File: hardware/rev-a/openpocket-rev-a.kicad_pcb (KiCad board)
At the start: 8 copper layers, 115 x 72 mm, 315 parts, among them J1 ER-TFT050A3-2 FFC, J11 5.8 GHz antenna U.FL, J12 push-push microSD, J13 speaker solder pads, J14 SSD1306 128x64 OLED pads, J15 expander developer pads, J18 rotary encoder control pads, J19 ARM switch pads, J2 USB-C, J20 AUX2 three-position switch pa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, J21 AUX3 three-position switch pa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, J22 AUX4 three-position switch pa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, J23 AIL trim pads, J24 ELE trim pads, J25 THR trim pads, J26 RUD trim pads, J3 battery/NTC, J4 speaker connector, J5 master switch, J6 ELRS, J7 left gimbal, J8 right gimbal, J9 menu/UI control pads, Q1 dual protection FET, Q2 Q_BUZZ buzzer MOSFET, U1 ESP32-S3-MINI-1U-N8, U10 display 3V3 buck, U11 analog OSD, U12 OSD 3V3-to-5V, U13 OSD 5V-to-3V3, U14 CVBS TFT controller, U15 AMT boot flash, U16 AMT flash mux, U17 backlight boost, U18 GPIO expander 0x20, U19 GPIO expander 0x21, U2 1S charger/power path, U20 master load switch, U21 I2S speaker amplifier, U22 3V3_SD load switch, U3 1S protector, U4 fuel gauge, U5 3V3 buck-boost, U6 5V boost, U7 5V_VIDEO load switch, U8 5V_DISPLAY load switch, U9 5V_ELRS load switch, Y1 27.000MHz, Y2 27.000MHz

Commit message: fix(rev-a): eliminate placement and silkscreen DRC violations
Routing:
- net AMT_FLASH_C_MISO: track 29.3 -> 0.00 mm, vias 2 -> 0
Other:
- board text removed: "5.8G U.FL"
- board text removed: "DEV IO"

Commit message: route(rev-a): connect U5 output bulk capacitor
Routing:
- net 3V3_LOGIC: track 0.00 -> 5.72 mm, vias 0 -> 1
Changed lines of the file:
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@@
+	)
+	(segment
+		(start 65.4 42.54)
+		(end 67 42)
+		(width 0.4)
+		(layer "F.Cu")
+		(net 2)
+	)
+	(via
+		(at 67 42)
+		(size 0.55)
+		(drill 0.25)
+		(layers "F.Cu" "B.Cu")
+		(tenting front back)
+		(net 2)
+	)
+	(segment
+		(start 67 42)
+		(end 67.035 46.035)
+		(width 0.4)
+		(layer "B.Cu")
+		(net 2)
 	)
 	(segment
@@
 	)
 	(via
-		(at 12.64 63.4)
+		(at 16.35 57.8)
 		(size 0.45)
 		(drill 0.2)
@@
 	)
 	(via
-		(at 16.35 57.8)
+		(at 12.64 63.4)
 		(size 0.45)
 		(drill 0.2)
@@
 	)
 	(segment
-		(start 7.8 66.3)
-		(end 2 66.3)
+		(start 2 66.3)
+		(end 2 43.2)
 		(width 0.4)
 		(layer "In2.Cu")
@@
 	)
 	(segment
-		(start 2 66.3)
-		(end 2 43.2)
+		(start 7.8 66.3)
+		(end 2 66.3)
 		(width 0.4)
 		(layer "In2.Cu")

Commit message: route(rev-a): extend reviewed 3V3 bulk fanout
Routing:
- net 3V3_LOGIC: track 5.72 -> 13.0 mm, vias 1 -> 3
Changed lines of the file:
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@@
+	)
+	(via
+		(at 62 48.5)
+		(size 0.55)
+		(drill 0.25)
+		(layers "F.Cu" "B.Cu")
+		(tenting front back)
+		(net 2)
 	)
 	(via
@@
 		(layers "F.Cu" "B.Cu")
 		(tenting front back)
+		(net 2)
+	)
+	(via
+		(at 66.5 47.5)
+		(size 0.55)
+		(drill 0.25)
+		(layers "F.Cu" "B.Cu")
+		(tenting front back)
+		(net 2)
+	)
+	(segment
+		(start 67.035 46.035)
+		(end 66.5 47.5)
+		(width 0.4)
+		(layer "B.Cu")
+		(net 2)
+	)
+	(segment
+		(start 62 48.5)
+		(end 63 49)
+		(width 0.4)
+		(layer "B.Cu")
 		(net 2)
 	)
@@
 	)
 	(segment
-		(start 16.35 57.8)
-		(end 16.35 56.95)
-		(width 0.3)
-		(layer "F.Cu")
-		(net 49)
+		(start 66.5 47.5)
+		(end 62 48.5)
+		(width 0.4)
+		(layer "In2.Cu")
+		(net 2)
 	)
 	(segment
@@
 		(net 49)
 	)
-	(via
-		(at 16.35 57.8)
-		(size 0.45)
-		(drill 0.2)
-		(layers "F.Cu" "B.Cu")
-		(tenting front back)
+	(segment
+		(start 16.35 57.8)
+		(end 16.35 56.95)
+		(width 0.3)
+		(layer "F.Cu")
 		(net 49)
 	)
@@
 		(net 49)
 	)
+	(via
+		(at 16.35 57.8)
+		(size 0.45)
+		(drill 0.2)
+		(layers "F.Cu" "B.Cu")
+		(tenting front back)
+		(net 49)
+	)
+	(segment
+		(start 12.64 63.4)
+		(end 16.35 57.8)
+		(width 0.4)
+		(layer "In2.Cu")
+		(net 49)
+	)
 	(segment
 		(start 10.6 64.5)
@@
 		(start 10.6 68.4)
 		(end 10.6 64.5)
-		(width 0.4)
-		(layer "In2.Cu")
-		(net 49)
-	)
-	(segment
-		(start 12.64 63.4)
-		(end 16.35 57.8)
 		(width 0.4)
 		(layer "In2.Cu")
@@
 	)
 	(via
+		(at 7.8 68.4)
+		(size 0.45)
+		(drill 0.2)
+		(layers "F.Cu" "B.Cu")
+		(tenting front back)
+		(net 53)
+	)
+	(via
 		(at 2 43.2)
 		(size 0.45)
@@
 		(net 53)
 	)
-	(via
-		(at 7.8 68.4)
-		(size 0.45)
-		(drill 0.2)
-		(layers "F.Cu" "B.Cu")
-		(tenting front back)
+	(segment
+		(start 7.8 66.3)
+		(end 2 66.3)
+		(width 0.4)
+		(layer "In2.Cu")
 		(net 53)
 	)
@@
 		(width 0.4)
 		(layer "In2.Cu")
-		(net 53)
-	)
-	(segment
-		(start 7.8 66.3)
-		(end 2 66.3)
-		(width 0.4)
-		(layer "In2.Cu")

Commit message: route(rev-a): add dedicated 3V3 distribution plane
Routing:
- net 3V3_LOGIC: track 13.0 -> 56.5 mm, vias 3 -> 54
- added copper zone on In5.Cu, net 3V3_LOGIC

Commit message: route(rev-a): add main 5V distribution plane
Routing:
- net SYS_SWITCHED_5V: track 0.00 -> 13.8 mm, vias 0 -> 15
- added copper zone on In2.Cu, net SYS_SWITCHED_5V

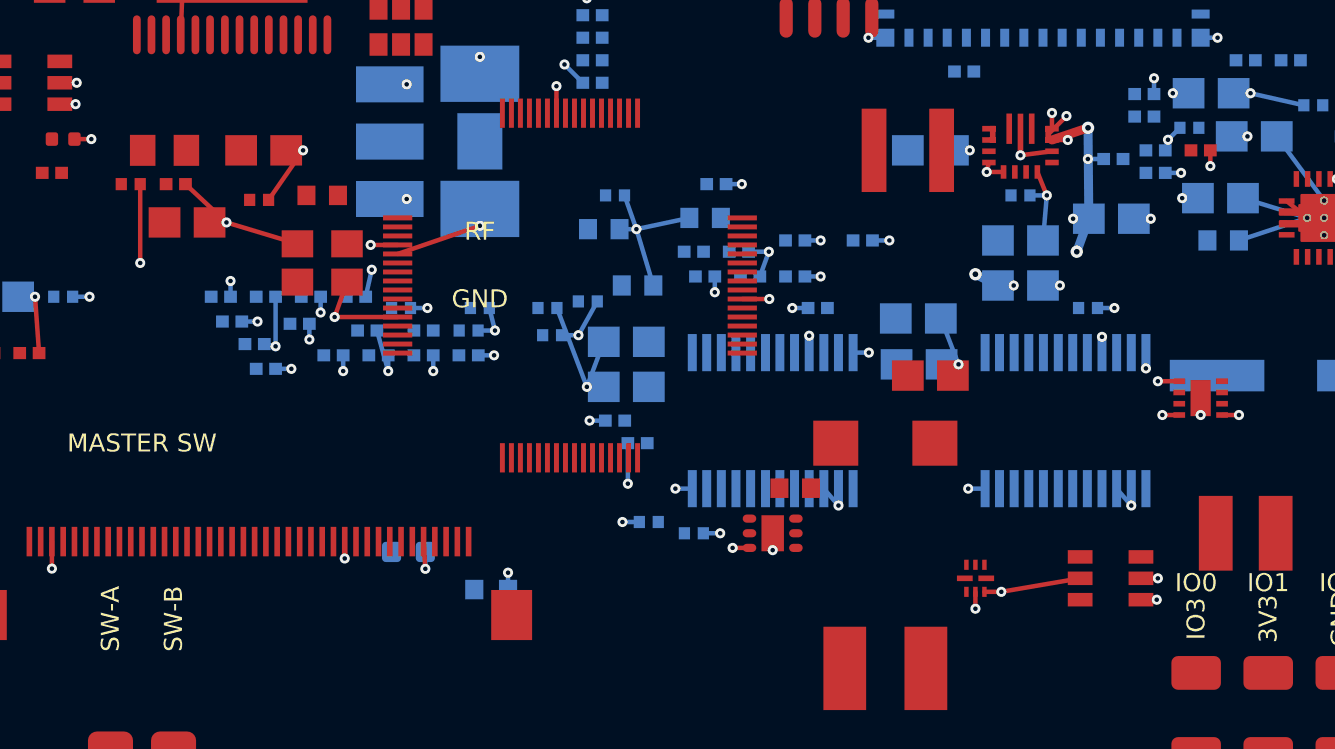
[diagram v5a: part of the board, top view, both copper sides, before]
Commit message: place(rev-a): cluster master switch with power converters
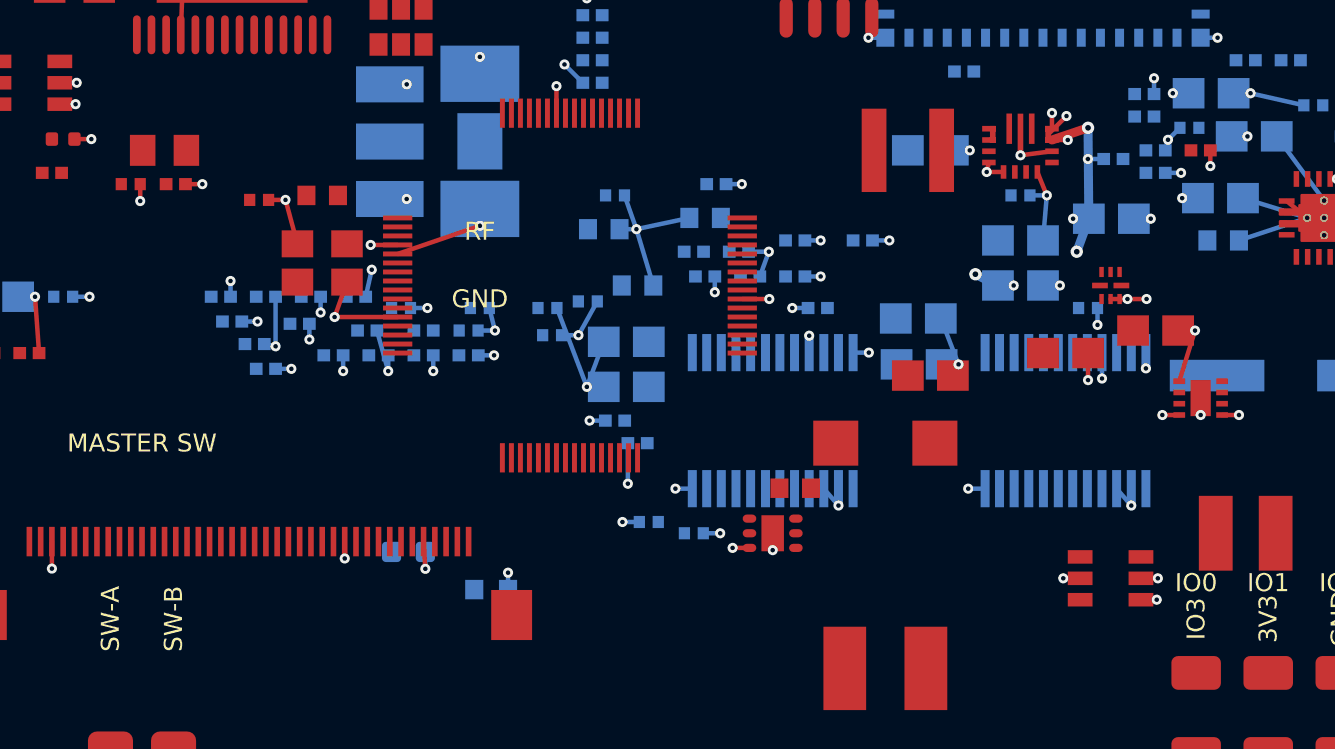
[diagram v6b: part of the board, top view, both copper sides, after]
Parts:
- moved C3 43.3 mm to (70.0, 51.0)
- moved C2 36.7 mm to (66.0, 52.0)
- moved U20 14.3 mm to (68.0, 49.0)
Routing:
- net GND: track 260.7 -> 252.5 mm, vias 144 -> 146

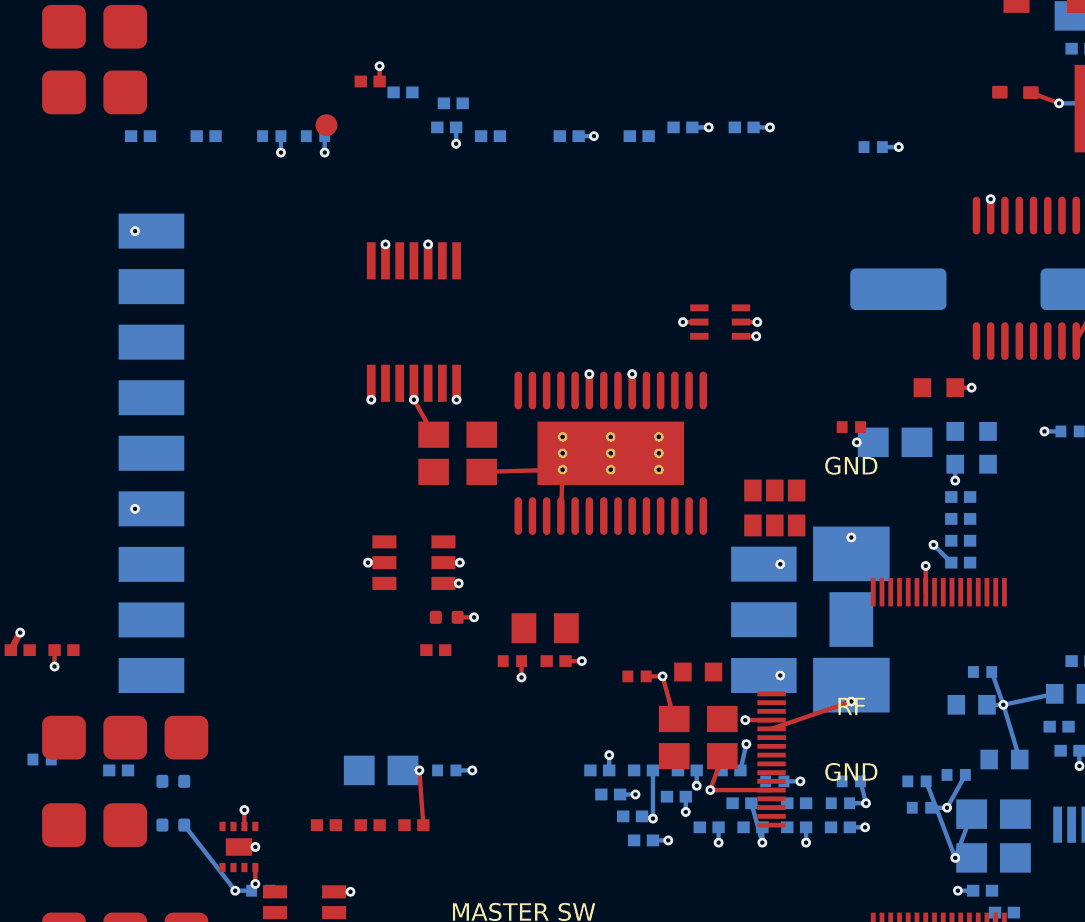
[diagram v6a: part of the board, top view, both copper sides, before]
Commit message: route(rev-a): add filtered video power island
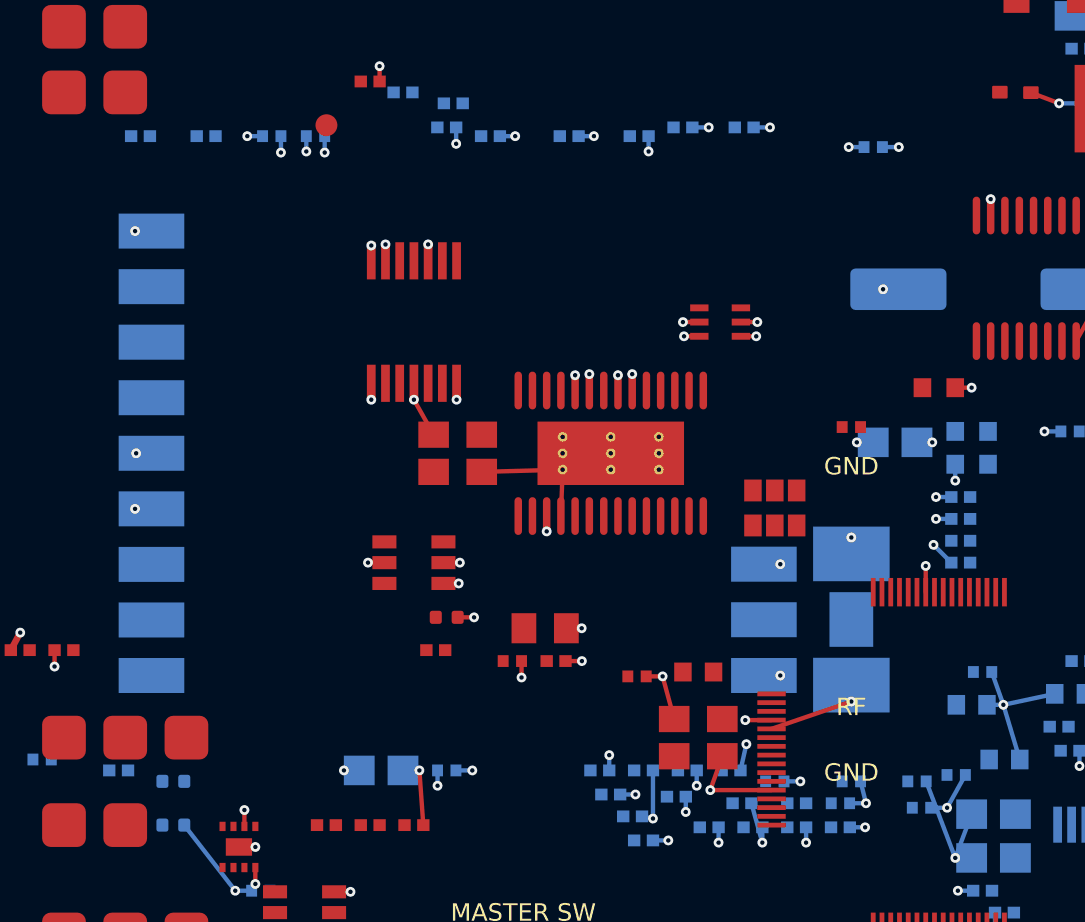
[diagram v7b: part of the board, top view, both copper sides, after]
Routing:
- net 5V_VIDEO_FILT: track 0.00 -> 12.6 mm, vias 0 -> 18
- added copper zone on In3.Cu, net 5V_VIDEO_FILT

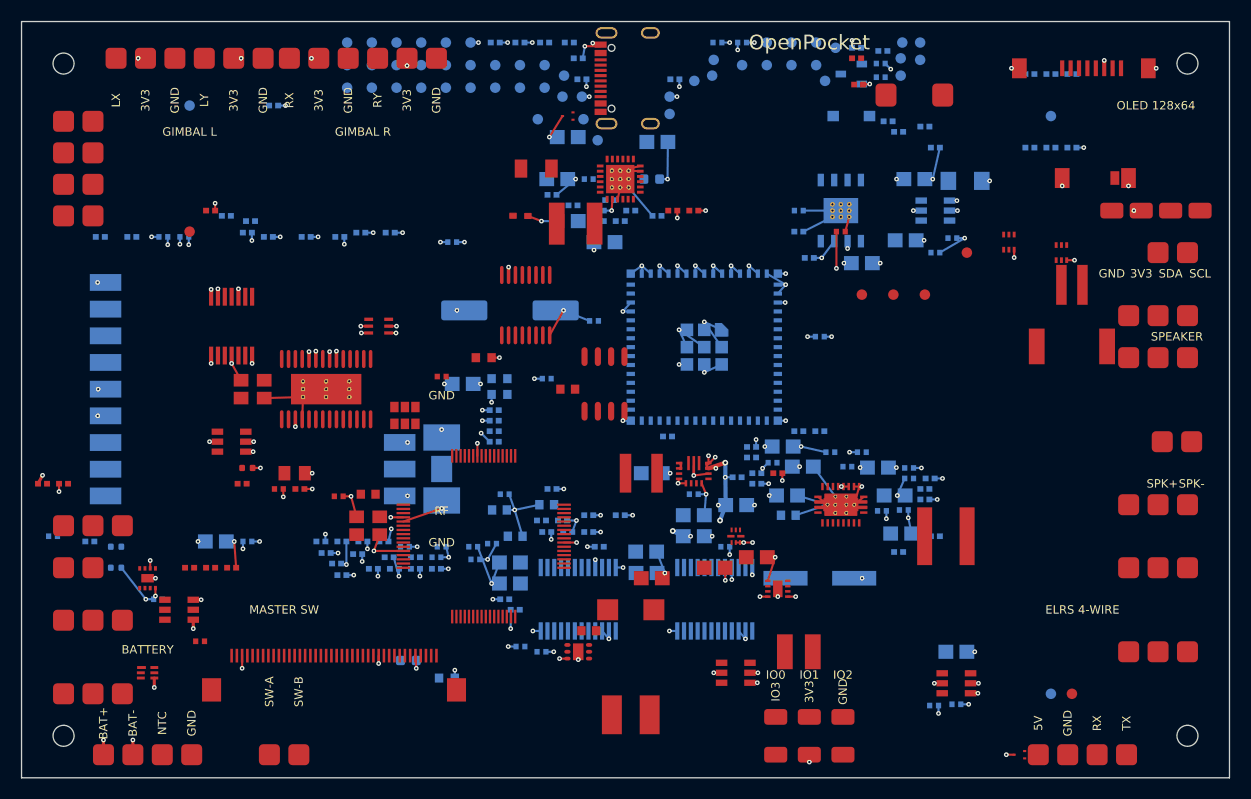
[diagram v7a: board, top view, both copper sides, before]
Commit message: route(rev-a): add display and SD power islands
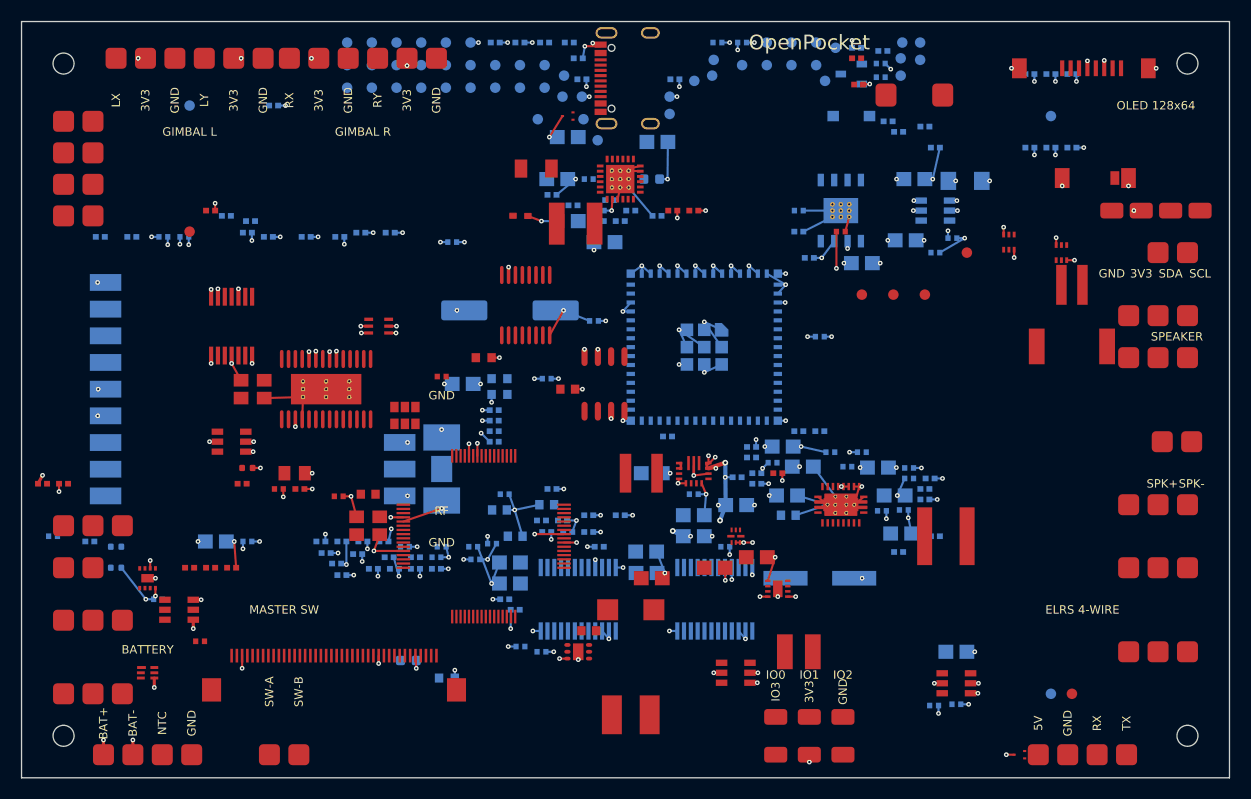
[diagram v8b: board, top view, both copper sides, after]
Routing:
- net DISPLAY_3V3_D: track 0.00 -> 9.55 mm, vias 0 -> 10
- net 3V3_SD: track 0.00 -> 8.40 mm, vias 0 -> 12
- added copper zone on In3.Cu, net 3V3_SD
- added copper zone on In4.Cu, net DISPLAY_3V3_D
